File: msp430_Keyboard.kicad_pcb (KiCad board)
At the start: 2 copper layers, 285.2 x 94.9 mm, 148 parts, among them SW1 `, SW10 2, SW11 W, SW12 S, SW13 Y, SW14 L_Super, SW15 3, SW16 E, SW17 D, SW18 X, SW19 4, SW2 TAB, SW20 R, SW21 F, SW22 C, SW23 5, SW24 T, SW25 G, SW26 V, SW27 6, SW28 Z, SW29 H, SW3 ESC, SW30 B, SW31 Space, SW32 7, SW33 U, SW34 J, SW35 N, SW36 8, SW37 I, SW38 K, SW39 M, SW4 L_Ctrl, SW40 9, SW41 O, SW42 L, SW43 ,, SW44 0, SW45 P, SW46 ;, SW47 ., SW48 R_Ctrl, SW49 -, SW5 L_Shift, SW50 [, SW51 ', SW52 /, SW53 R_Shift, SW54 =, SW55 ], SW56 \, SW57 Alt_GR, SW58 Backspace, SW59 Enter, SW6 1, SW60 R_Super, SW61 FUNC, SW7 Q, SW8 A, SW9 L_Alt, U1 MSP430F5510IRGZ, U2 74LS138, U3 74LS138

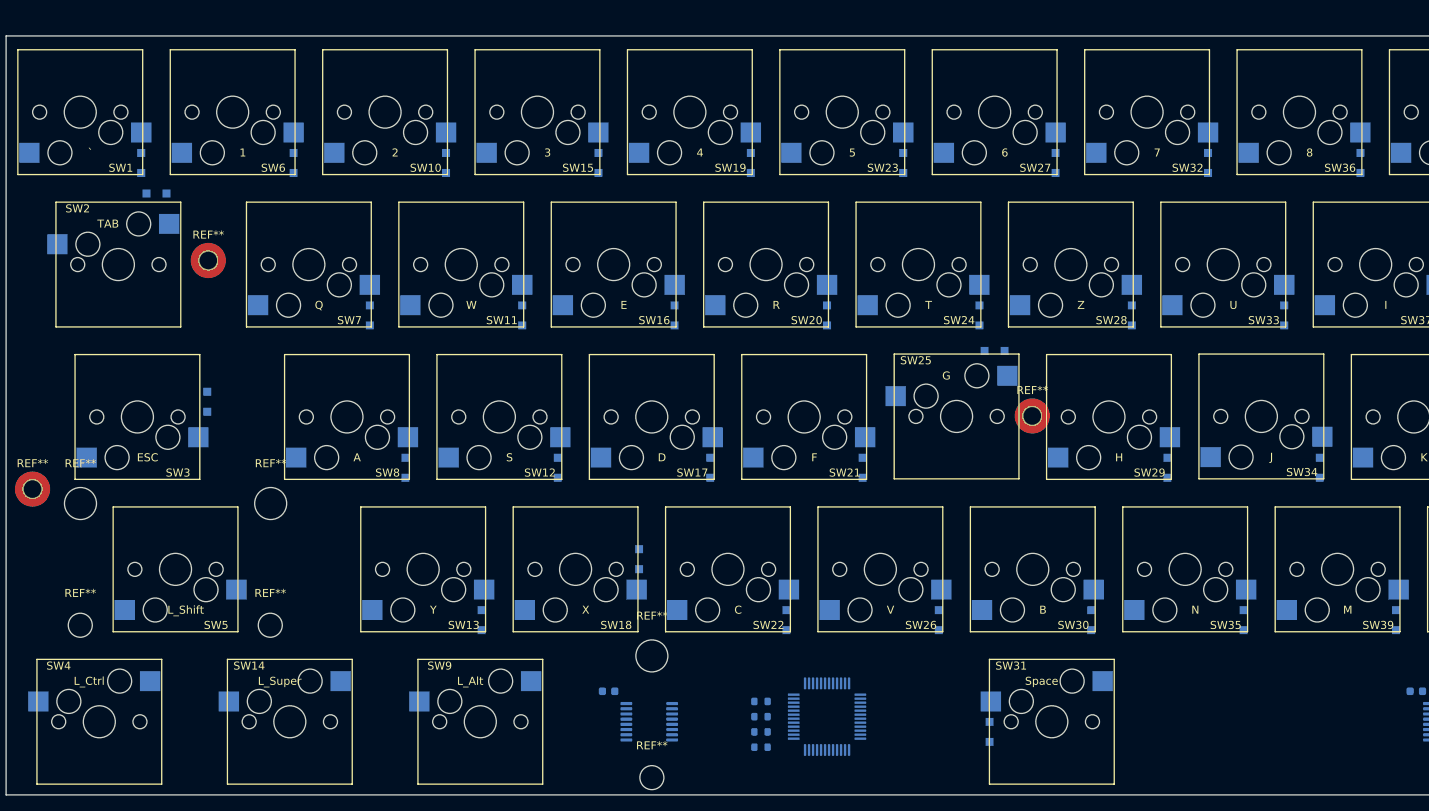
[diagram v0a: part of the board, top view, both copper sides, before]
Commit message: USB-Part und ESP32
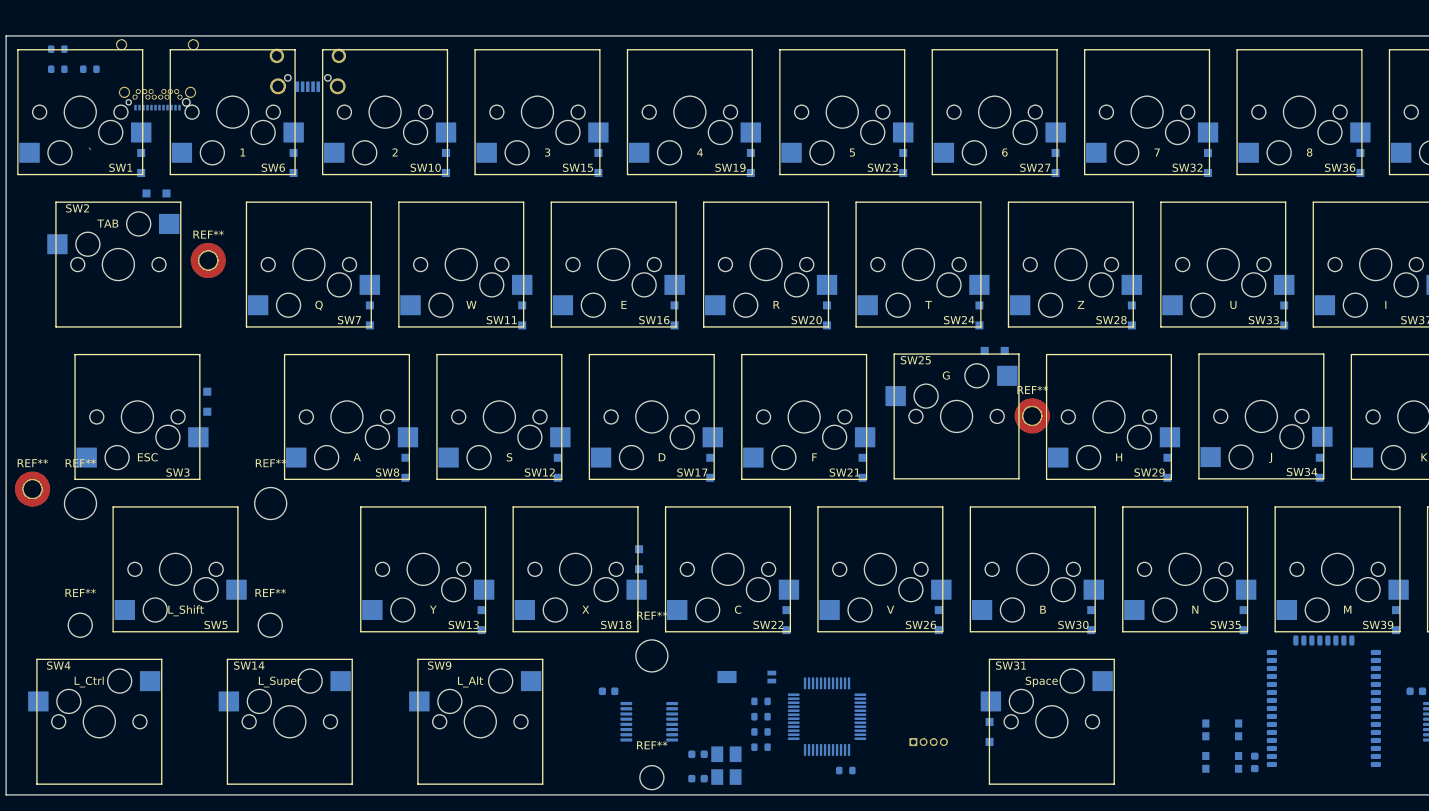
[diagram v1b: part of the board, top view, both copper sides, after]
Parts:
- added C3: C_Small, Capacitor_SMD:C_0603_1608Metric, B.Cu at (77.2, 83.3)
- added C4: C_Small, Capacitor_SMD:C_0603_1608Metric, B.Cu at (77.2, 80.3)
- added C5: C_Small, Capacitor_SMD:C_0603_1608Metric, B.Cu at (146.8, 81.3)
- added J1: Conn_01x04_Male, Connector_PinHeader_1.27mm:PinHeader_1x04_P1.27mm_Horizontal, B.Cu at (104.1, 78.7)
- added J2: USB_C_Receptacle_USB2.0, Connector_USB:USB_C_Receptacle_Amphenol_12401548E4-2A_CircularHoles, B.Cu at (9.65, -5.59)
- added R5: 1k4, Resistor_SMD:R_0603_1608Metric, B.Cu at (95.7, 82.3)
- added R6: 1Meg, Resistor_SMD:R_0603_1608Metric, B.Cu at (-2.81, -5.37)
- added R7: 5k1, Resistor_SMD:R_0603_1608Metric, B.Cu at (-2.81, -7.88)
- added R8: 5k1, Resistor_SMD:R_0603_1608Metric, B.Cu at (1.20, -5.37)
- added REF**: USB_Micro-B_Wuerth_629105150521_CircularHoles, Connector_USB:USB_Micro-B_Wuerth_629105150521_CircularHoles, B.Cu at (28.4, -5.08)
- added SW62: SW_Push, Button_Switch_SMD:SW_Push_1P1T_NO_CK_KMR2, B.Cu at (142.7, 81.3)
- added SW63: SW_Push, Button_Switch_SMD:SW_Push_1P1T_NO_CK_KMR2, B.Cu at (142.7, 77.2)
- added U4: Micro-32-HS-Wismar, HS-Wismar:micro32, B.Cu at (155.4, 66.0)
- added Y1: 12MHz, Crystal:Crystal_SMD_EuroQuartz_MT-4Pin_3.2x2.5mm_HandSoldering, B.Cu at (80.8, 81.7)
- added Y2: 32.768kHz, Crystal:Crystal_SMD_MicroCrystal_MS3V-T1R, B.Cu at (83.3, 70.6)
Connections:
- U1 pad 10: Net-(U1-Pad10) -> GND
- U1 pad 11: Net-(U1-Pad11) -> +3V3
- U1 pad 12: Net-(U1-Pad12) -> GND
- U1 pad 27: Net-(U1-Pad27) -> GND
- U1 pad 28: Net-(U1-Pad28) -> +3V3
- U1 pad 29: Net-(U1-Pad29) -> /esp32/EN_\RST
- U1 pad 30: Net-(U1-Pad30) -> /esp32/TX_out
- U1 pad 31: Net-(U1-Pad31) -> /esp32/RX_in
- U1 pad 37: Net-(U1-Pad37) -> GND
- U1 pad 38: Net-(U1-Pad38) -> /USB/D+
- U1 pad 40: Net-(U1-Pad40) -> /USB/D-
- U1 pad 41: Net-(U1-Pad41) -> VBUS
- U1 pad 42: Net-(U1-Pad42) -> +3V3
- U1 pad 44: Net-(U1-Pad44) -> GND
- U1 pad 7: Net-(U1-Pad7) -> +3V3

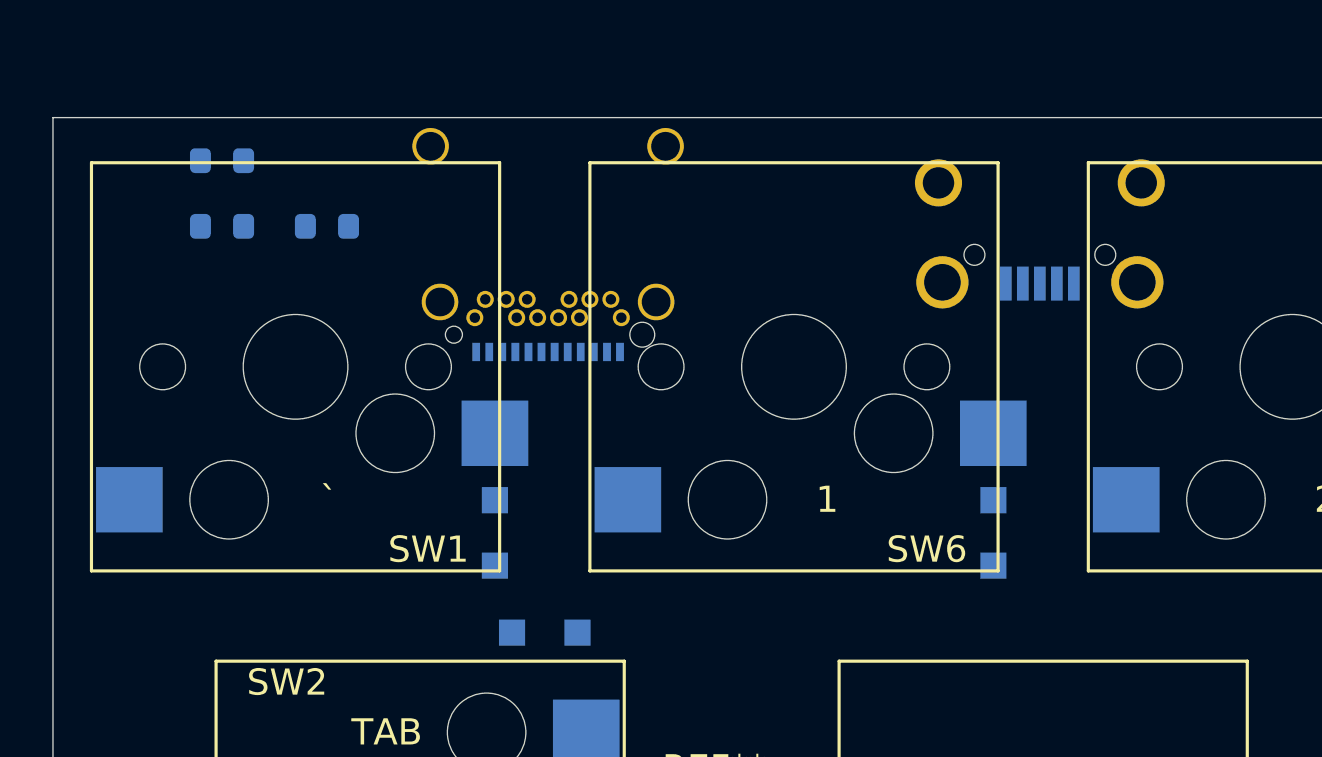
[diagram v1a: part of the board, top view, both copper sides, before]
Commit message: Rotated Keys to make room for USB-C-Port
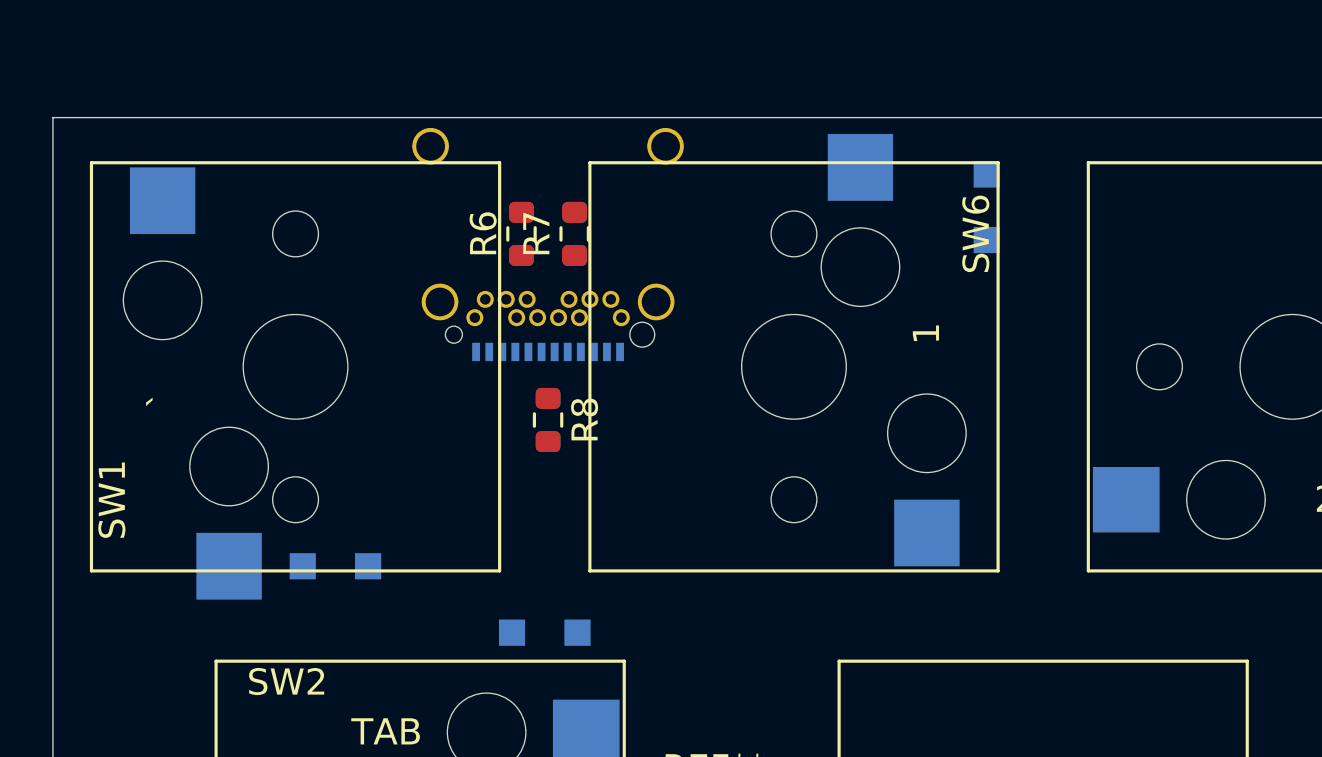
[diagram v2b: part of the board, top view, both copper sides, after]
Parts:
- removed the REF** at (28.4, -5.08)
- R6, R7, R8: moved to F.Cu
- moved R7 13.8 mm to (10.7, -5.08), turned to 90 degrees
- moved D4 12.4 mm to (26.4, -6.10)
- moved R6 11.4 mm to (8.64, -5.08), turned to 90 degrees
- moved R8 11.2 mm to (9.65, 2.03), turned to 270 degrees
- moved D1 6.23 mm to (1.52, 7.62), turned to 180 degrees
- turned SW1 to 90 degrees
- turned SW6 to 270 degrees

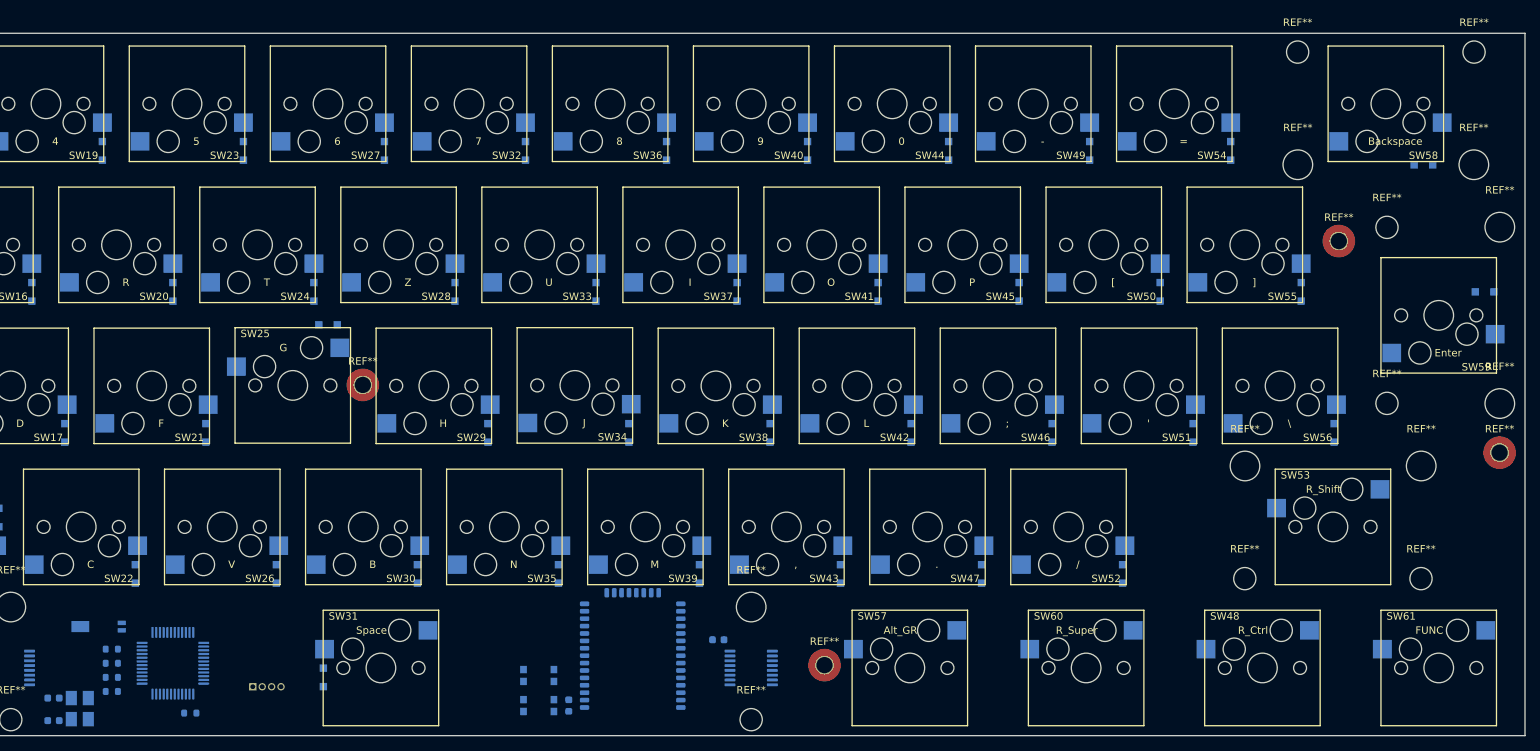
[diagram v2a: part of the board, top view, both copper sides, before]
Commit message: Rotary Encoder added
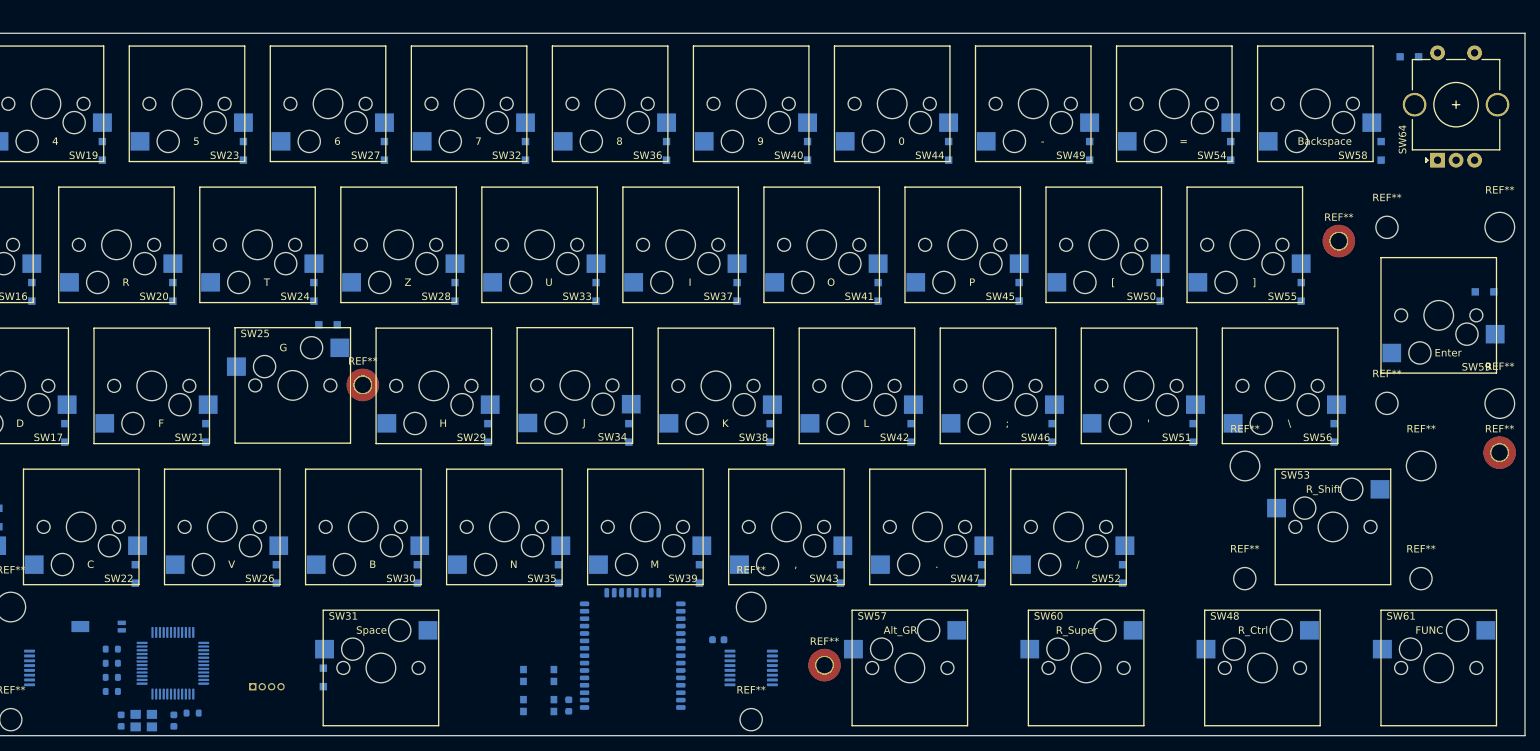
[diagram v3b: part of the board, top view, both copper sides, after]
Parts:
- removed the REF** at (269.1, 8.23)
- removed the REF** at (269.1, -6.99)
- removed the REF** at (245.3, -6.99)
- removed the REF** at (245.3, 8.23)
- added D53: D_Small, Diode_SMD:D_SOD-323_HandSoldering, B.Cu at (260.4, -6.35)
- added SW64: Rotary_Encoder_Switch, Rotary_Encoder:RotaryEncoder_Alps_EC11E-Switch_Vertical_H20mm_CircularMountingHoles, F.Cu at (264.2, 7.62)
- Y1: footprint Crystal:Crystal_SMD_EuroQuartz_MT-4Pin_3.2x2.5mm_HandSoldering -> Crystal:Crystal_SMD_3225-4Pin_3.2x2.5mm
- moved C3 16.3 mm to (93.5, 83.3), turned to 90 degrees
- moved C4 9.64 mm to (86.4, 83.3), turned to 270 degrees
- moved SW58 9.53 mm to (247.7, 0.00)
- moved Y1 8.79 mm to (89.4, 83.3), turned to 180 degrees
- moved D51 6.02 mm to (256.5, 6.35), turned to 90 degrees
- moved R5 0.32 mm to (96.0, 82.3)
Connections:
- U1 pad 22: Net-(SW61-Pad1) -> Net-(U1-Pad22)
- U1 pad 29: /esp32/EN_\RST -> /Switch_Matrix/A
- U1 pad 30: /esp32/TX_out -> /Switch_Matrix/B
- U1 pad 31: /esp32/RX_in -> /esp32/TX_out
- U1 pad 32: Net-(U1-Pad32) -> /esp32/RX_in
- U1 pad 5: Net-(U1-Pad5) -> Net-(SW61-Pad1)
- U1 pad 6: Net-(U1-Pad6) -> /esp32/EN_\RST
- Y1 pad 2: Net-(C4-Pad1) -> Net-(Y1-Pad2)
- Y1 pad 3: (no net) -> Net-(C4-Pad1)
- Y1 pad 4: (no net) -> Net-(Y1-Pad4)

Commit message: Routing angefangen
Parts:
- added C10: 220n, Capacitor_SMD:C_0603_1608Metric_Pad1.08x0.95mm_HandSolder, F.Cu at (93.6, 72.6)
- added C11: 100n, Capacitor_SMD:C_0603_1608Metric_Pad1.08x0.95mm_HandSolder, F.Cu at (94.9, 80.6)
- added C12: 10µ, Capacitor_SMD:C_1206_3216Metric_Pad1.33x1.80mm_HandSolder, F.Cu at (97.4, 76.8)
- added C13: 100n, Capacitor_SMD:C_0603_1608Metric_Pad1.08x0.95mm_HandSolder, F.Cu at (96.6, 80.6)
- added C14: 10µ, Capacitor_SMD:C_1206_3216Metric_Pad1.33x1.80mm_HandSolder, F.Cu at (94.9, 76.8)
- added C15: 100n, Capacitor_SMD:C_0603_1608Metric_Pad1.08x0.95mm_HandSolder, F.Cu at (93.1, 80.6)
- added C16: 10µ, Capacitor_SMD:C_1206_3216Metric_Pad1.33x1.80mm_HandSolder, F.Cu at (92.3, 76.8)
- added C17: 470n, Capacitor_SMD:C_0603_1608Metric_Pad1.08x0.95mm_HandSolder, F.Cu at (95.8, 83.1)
- added C18: 220n, Capacitor_SMD:C_0603_1608Metric_Pad1.08x0.95mm_HandSolder, F.Cu at (95.1, 72.6)
- added C6: 10µ, Capacitor_SMD:C_1206_3216Metric_Pad1.33x1.80mm_HandSolder, B.Cu at (104.5, 13.6)
- added C7: 10µ, Capacitor_SMD:C_1206_3216Metric_Pad1.33x1.80mm_HandSolder, B.Cu at (110.6, 13.5)
- added C8: 10µ, Capacitor_SMD:C_1206_3216Metric_Pad1.33x1.80mm_HandSolder, B.Cu at (101.2, 30.6)
- added C9: 10µ, Capacitor_SMD:C_1206_3216Metric_Pad1.33x1.80mm_HandSolder, B.Cu at (89.4, 32.0)
- added D54: LED_Small, LED_SMD:LED_0603_1608Metric_Pad1.05x0.95mm_HandSolder, F.Cu at (9.53, -8.13)
- added J3: Conn_01x02_Male, Connector_JST:JST_PH_S2B-PH-K_1x02_P2.00mm_Horizontal, B.Cu at (115.1, 13.3)
- added JP1: Jumper_NC_Small, Jumper:SolderJumper-2_P1.3mm_Bridged2Bar_RoundedPad1.0x1.5mm, F.Cu at (87.4, 82.7)
- added R10: 470, Resistor_SMD:R_0603_1608Metric_Pad0.98x0.95mm_HandSolder, F.Cu at (9.53, -6.60)
- added R9: 2k2, Resistor_SMD:R_0603_1608Metric_Pad0.98x0.95mm_HandSolder, B.Cu at (107.6, 11.8)
- added U5: MCP73831-2-OT, Package_TO_SOT_SMD:SOT-23-5, B.Cu at (107.6, 14.2)
- added U6: AMS1117-3.3, Package_TO_SOT_SMD:SOT-223-3_TabPin2, B.Cu at (95.2, 32.1)
- C5: moved to F.Cu
- J2: footprint Connector_USB:USB_C_Receptacle_Amphenol_12401548E4-2A_CircularHoles -> msp430_Keyboard:632723300011
- R6, R8: moved to B.Cu
- moved D53 26.0 mm to (238.3, 7.37), turned to 90 degrees
- moved Y2 20.7 mm to (101.7, 80.1), turned to 180 degrees
- moved C4 20.6 mm to (101.9, 69.7), turned to 90 degrees
- moved R1 20.5 mm to (104.6, 73.2), turned to 180 degrees
- moved R3 19.6 mm to (104.6, 74.5), turned to 180 degrees
- moved R2 17.1 mm to (101.9, 73.9), turned to 180 degrees
- moved R4 16.8 mm to (101.9, 75.3), turned to 180 degrees
- moved Y1 16.5 mm to (98.8, 69.7), turned to 0 degrees
- moved D2 16.3 mm to (11.9, 26.3), turned to 90 degrees
- moved D22 15.7 mm to (112.5, 45.5), turned to 90 degrees
- moved C3 13.8 mm to (95.9, 69.7), turned to 270 degrees
- moved D4 13.5 mm to (27.9, 7.37)
- moved R5 12.9 mm to (93.1, 69.7), turned to 90 degrees
- moved D11 9.44 mm to (66.0, 64.5), turned to 90 degrees
- moved D3 9.34 mm to (14.7, 45.5), turned to 90 degrees
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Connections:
- SW64 pad S1: Net-(R4-Pad1) -> Net-(R2-Pad1)
- U1 pad 42: +3V3 -> Net-(C10-Pad1)
- Y2 pad 1: Net-(U1-Pad8) -> Net-(U1-Pad9)
- Y2 pad 2: Net-(U1-Pad9) -> Net-(U1-Pad8)
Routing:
- net Net-(R2-Pad1): track 0.00 -> 332.8 mm
- net Net-(R3-Pad1): track 0.00 -> 301.9 mm
- net Net-(R1-Pad1): track 0.00 -> 284.0 mm
- net Net-(R4-Pad1): track 0.00 -> 206.1 mm
- net Net-(D53-Pad2): track 0.00 -> 37.3 mm
- net Net-(D1-Pad1): track 0.00 -> 32.5 mm
- net Net-(D4-Pad2): track 0.00 -> 19.6 mm
- net Net-(D22-Pad2): track 0.00 -> 12.6 mm
- net Net-(J2-PadS1): track 0.00 -> 11.6 mm
- net Net-(D2-Pad2): track 0.00 -> 11.4 mm
- net /USB/D+: track 0.00 -> 7.88 mm, vias 0 -> 1
- net Net-(D11-Pad2): track 0.00 -> 5.23 mm
- net /USB/D-: track 0.00 -> 4.65 mm, vias 0 -> 1
- net Net-(D6-Pad2): track 0.00 -> 3.60 mm
- net Net-(D50-Pad2): track 0.00 -> 3.60 mm
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- added copper zone on B.Cu, net GND
- added copper zone on F.Cu, net GND
